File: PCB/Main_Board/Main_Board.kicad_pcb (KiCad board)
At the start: 2 copper layers, 100.3 x 115.6 mm, 34 parts, among them J1 POWER_SUPPLY, J2 LIMIT_SWITCH, J3 ToF, J4 BUCK_IN, J5 BUCK_OUT, J6 ESP32_Left, J7 ESP32_Right, J8 CABLE, J9 MOTOR, U1 74AHCT125

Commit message: Updated boards
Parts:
- added R12: 10K, Resistor_THT:R_Axial_DIN0207_L6.3mm_D2.5mm_P7.62mm_Horizontal, F.Cu at (64.7, 112.5)
- C6: value 470uF -> 47uF
- R10, R11: value 1K -> 4.7K
- moved C6 0.33 mm to (100.0, 108.0)
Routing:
- net /LIMIT_SW: track 11.8 -> 26.4 mm
- net /3V3: track 116.2 -> 130.5 mm

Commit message: Added decoupling capacitor to AHCT
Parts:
- added C7: 0.1uF, Capacitor_THT:C_Rect_L7.2mm_W3.5mm_P5.00mm_FKS2_FKP2_MKS2_MKP2, F.Cu at (82.5, 59.0)
- moved R1 10.3 mm to (70.5, 50.0)
- moved C2 3.44 mm to (81.5, 50.0)
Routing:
- net /+5V: track 104.6 -> 107.8 mm
- net Net-(J6-Pin_4): track 12.4 -> 15.0 mm
- net /BTNS: track 101.7 -> 99.9 mm
- net GND: vias 0 -> 12

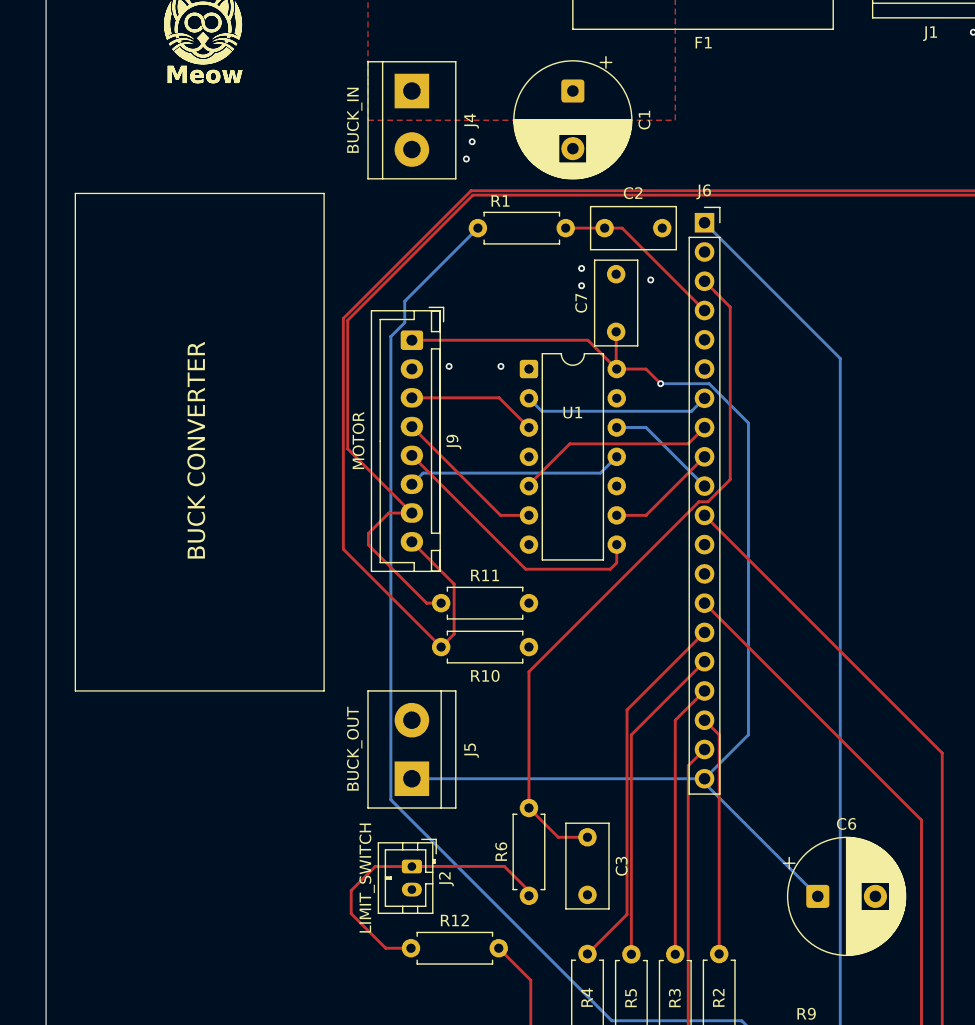
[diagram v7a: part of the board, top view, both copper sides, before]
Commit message: Add junctions and wires for improved connectivity on Main Board schematic
- Introduced multiple junctions at specified coordinates to enhance circuit connections.
- Updated wire connections to reflect new junction placements and ensure proper routing.
- Adjusted component positions and labels for clarity and consistency.
- Added two resistors (R13 and R14) with specified values and footprints to the schematic.
- Updated GND symbol and its properties to align with new layout.
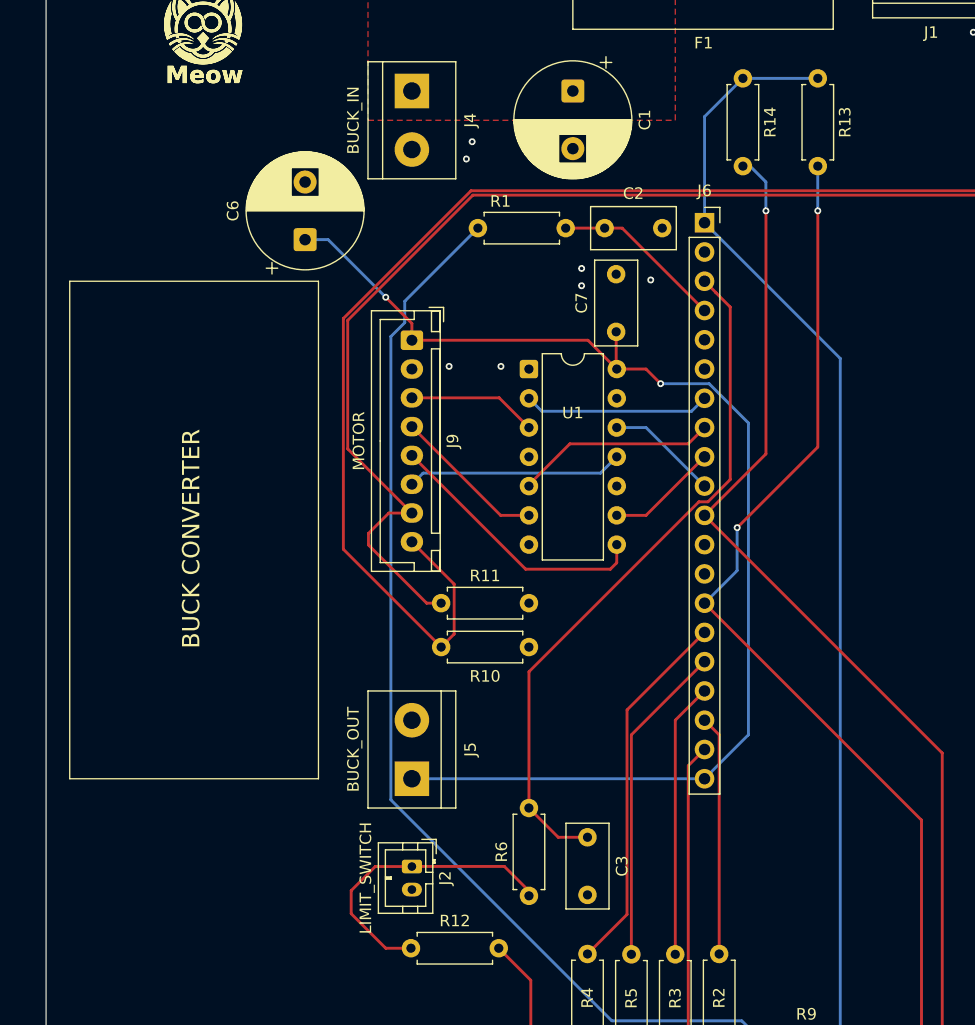
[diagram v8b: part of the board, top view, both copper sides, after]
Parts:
- added R13: 10K, Resistor_THT:R_Axial_DIN0207_L6.3mm_D2.5mm_P7.62mm_Horizontal, F.Cu at (100.0, 37.0)
- added R14: 10K, Resistor_THT:R_Axial_DIN0207_L6.3mm_D2.5mm_P7.62mm_Horizontal, F.Cu at (93.5, 37.0)
- moved C6 72.3 mm to (55.5, 51.0), turned to 90 degrees
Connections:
- net /LIMIT_SW renamed Net-(J2-Pin_1)
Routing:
- net /I2C_SCL: track 51.7 -> 93.7 mm, vias 0 -> 2
- net /I2C_SDA: track 60.0 -> 93.7 mm, vias 0 -> 1
- net /3V3: track 130.5 -> 151.0 mm
- net /+5V: track 107.8 -> 107.7 mm, vias 1 -> 2
